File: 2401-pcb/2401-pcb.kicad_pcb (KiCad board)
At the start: 2 copper layers, 33 parts, among them J1 Conn_01x04_Female, Q1 SFH3710, Q2 SFH3710, SW1 SW_SPDT, U1 TLV70228_SOT23-5, U2 VL6180X, U3 LIS3DH, U4 LMV321, U5 LMV321, U6 INA126, U7 DPS422, U8 AT25SF641-SUB-T, U9 STM32G070KBT6

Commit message: Improve schematics
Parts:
- removed the C6 at (135.9, 108.6)
- added C13: 4.7uF, Capacitor_SMD:C_0805_2012Metric, F.Cu at (175.0, 106.0)
- added C14: 100nF, Capacitor_SMD:C_0603_1608Metric, F.Cu at (170.0, 80.0)
- added C3: 100nF, Capacitor_SMD:C_0603_1608Metric, F.Cu at (165.0, 123.0)
- added C5: CP1_Small, Capacitor_SMD:CP_Elec_4x5.4, F.Cu at (159.1, 124.7)
- added D3: Red, LED_SMD:LED_0805_2012Metric, F.Cu at (165.8, 80.2)
- added D4: Green, LED_SMD:LED_0805_2012Metric, F.Cu at (170.5, 77.2)
- added J2: Conn_ARM_JTAG_SWD_10, Jitter_Footprints:connector_jtag_10pin_shrouded, F.Cu at (89.0, 107.0)
- added J3: Conn_01x04_Male, Connector_PinHeader_2.54mm:PinHeader_1x04_P2.54mm_Vertical, F.Cu at (178.0, 124.0)
- added R10: 4k7, Resistor_SMD:R_0805_2012Metric_Pad1.15x1.40mm_HandSolder, F.Cu at (161.2, 80.1)
- added R11: 150, Resistor_SMD:R_0805_2012Metric_Pad1.15x1.40mm_HandSolder, F.Cu at (165.9, 77.2)
- added R12: 150, Resistor_SMD:R_0805_2012Metric_Pad1.15x1.40mm_HandSolder, F.Cu at (170.7, 74.2)
- added R3: 47k, Resistor_SMD:R_0805_2012Metric_Pad1.15x1.40mm_HandSolder, F.Cu at (169.0, 113.0)
- added R4: 47k, Resistor_SMD:R_0805_2012Metric_Pad1.15x1.40mm_HandSolder, F.Cu at (173.8, 113.0)
- added R7: 4k7, Resistor_SMD:R_0805_2012Metric_Pad1.15x1.40mm_HandSolder, F.Cu at (161.2, 74.2)
- added R8: 4k7, Resistor_SMD:R_0805_2012Metric_Pad1.15x1.40mm_HandSolder, F.Cu at (161.2, 77.2)
- added R9: 4k7, Resistor_SMD:R_0805_2012Metric_Pad1.15x1.40mm_HandSolder, F.Cu at (165.9, 74.2)
- C2: value 100nF -> 4.7uF; footprint Capacitor_SMD:C_0603_1608Metric -> Capacitor_SMD:C_0805_2012Metric
- moved U8 5.00 mm to (164.0, 97.0)
- renumbered C8 to C10, C3 to C11, C4 to C12, C12 to C15, C5 to C4, C11 to C6, C9 to C8, C10 to C9, R3 to R5, R4 to R6, U3 to U1, U6 to U3, U7 to U5, U5 to U6, U1 to U7, U9 to U8, U8 to U9
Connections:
- net Net-(BT1-Pad1) renamed Vbatt
- U1 pad 11: (no net) -> /accel_int1
- U1 pad 4: (no net) -> /SCL
- U1 pad 6: (no net) -> /SDA
- U1 pad 8: (no net) -> +2V8
- U1 pad 9: (no net) -> /accel_int2
- U2 pad 1: (no net) -> /distance_int
- U2 pad 4: (no net) -> Net-(R3-Pad2)
- U2 pad 5: (no net) -> /SCL
- U2 pad 6: (no net) -> /SDA
- U3 pad 6: (no net) -> /load_cell
- U4 pad 2: +2V8 -> GND
- U4 pad 5: GND -> +2V8
- U5 pad 2: (no net) -> +2V8
- U5 pad 3: (no net) -> /SDA
- U5 pad 4: (no net) -> /SCL
- U5 pad 5: (no net) -> GND
- U6 pad 2: +2V8 -> GND
- U6 pad 5: GND -> +2V8
- U8 pad 1: (no net) -> /LED_RED
- U8 pad 10: (no net) -> /photo_diode_2
- U8 pad 11: (no net) -> /load_cell
- U8 pad 12: (no net) -> /FLASH_SCLK
- U8 pad 13: (no net) -> /FLASH_MISO
- U8 pad 14: (no net) -> /FLASH_MOSI
- U8 pad 15: (no net) -> /Vbatt_sense
- U8 pad 16: (no net) -> /distance_int
- U8 pad 17: (no net) -> /accel_int1
- U8 pad 18: (no net) -> /~FLASH_CS
- U8 pad 19: (no net) -> /Tx
- U8 pad 21: (no net) -> /Rx
- U8 pad 24: (no net) -> /SWDIO
- U8 pad 25: (no net) -> /SWCLK
- U8 pad 27: (no net) -> /accel_int2
- U8 pad 30: (no net) -> /SCL
- U8 pad 31: (no net) -> /SDA
- U8 pad 32: (no net) -> /LED_GREEN
- U8 pad 4: (no net) -> +2V8
- U8 pad 5: (no net) -> GND
- U8 pad 6: (no net) -> /~RST
- U8 pad 7: (no net) -> /photo_transistor_1
- U8 pad 8: (no net) -> /photo_transistor_2
- U8 pad 9: (no net) -> /photo_diode_1
- U9 pad 1: (no net) -> /~FLASH_CS
- U9 pad 2: (no net) -> /FLASH_MISO
- U9 pad 3: (no net) -> +2V8
- U9 pad 5: (no net) -> /FLASH_MOSI
- U9 pad 6: (no net) -> /FLASH_SCLK
- U9 pad 7: (no net) -> +2V8

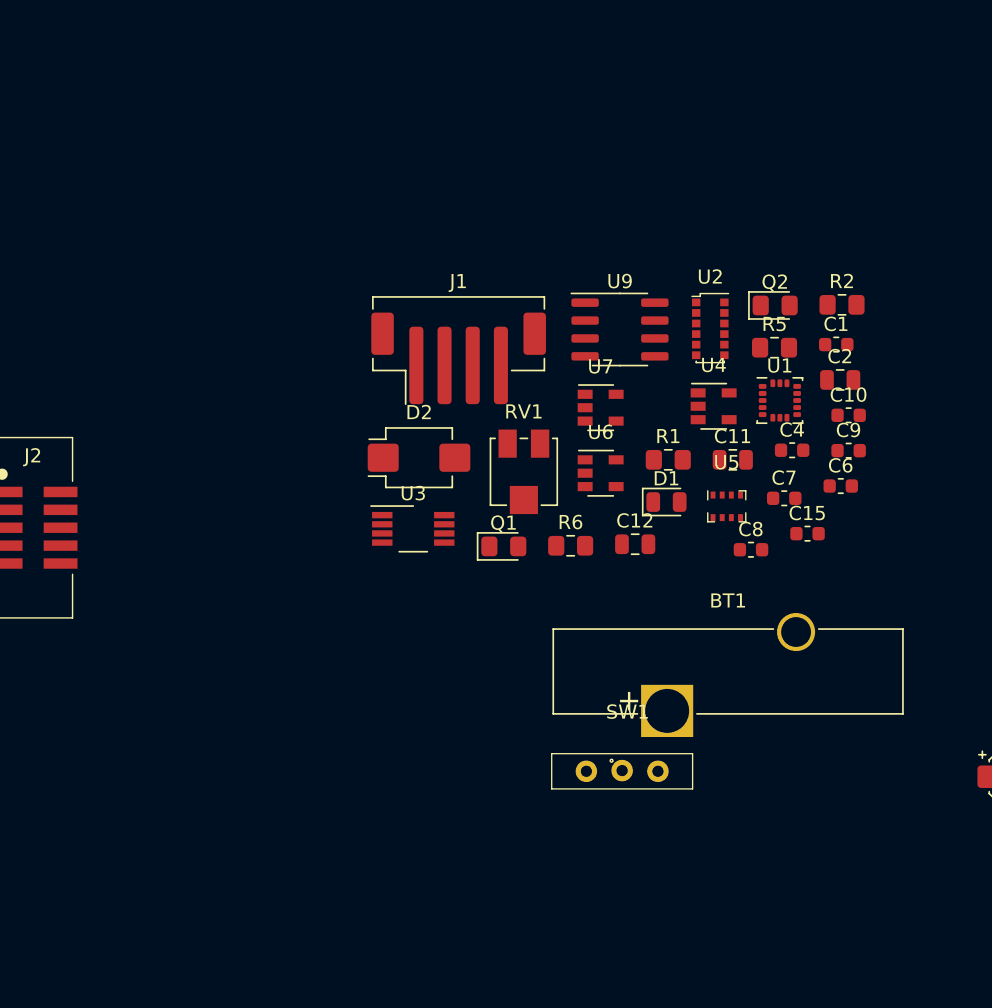
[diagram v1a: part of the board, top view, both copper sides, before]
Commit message: PCB: assign/fix footprints + 3D
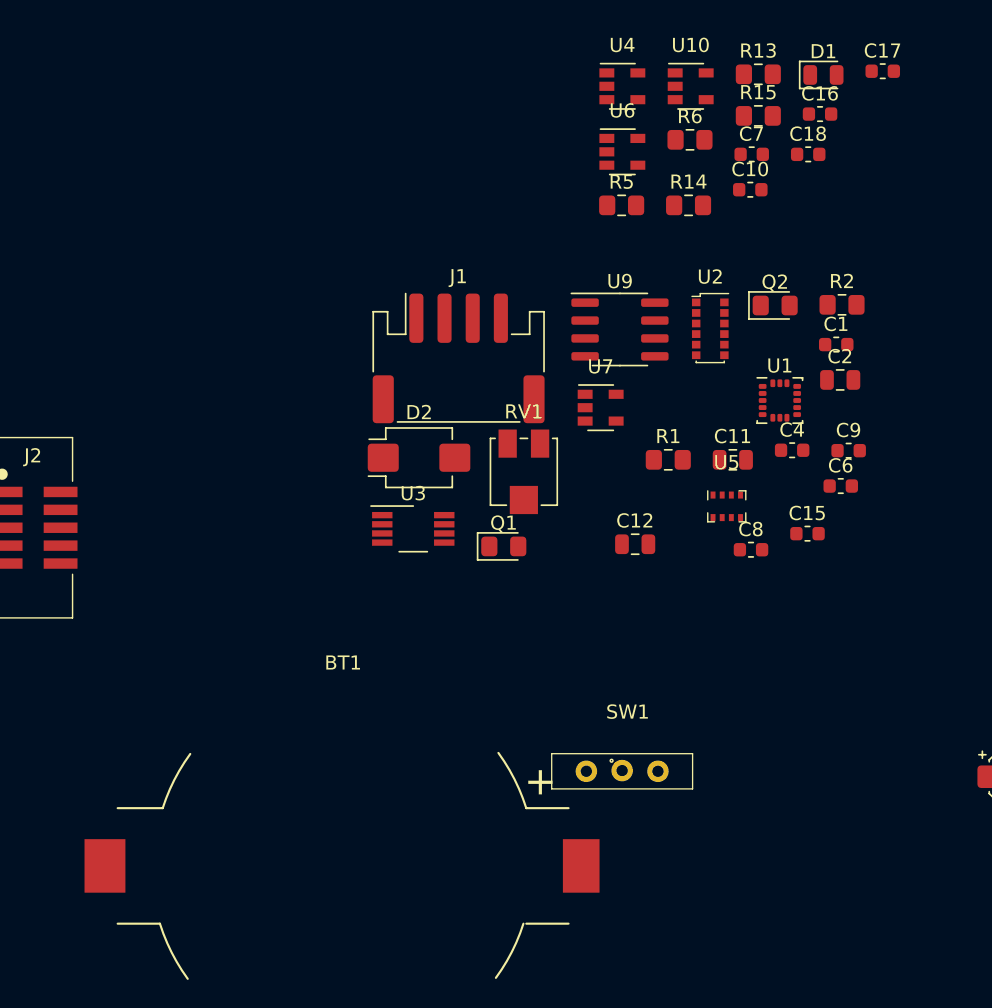
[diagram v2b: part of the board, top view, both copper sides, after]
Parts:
- added C16: 100nF, Capacitor_SMD:C_0603_1608Metric, F.Cu at (144.8, 77.6)
- added C17: 15pF, Capacitor_SMD:C_0603_1608Metric, F.Cu at (149.3, 74.6)
- added C18: 100nF, Capacitor_SMD:C_0603_1608Metric, F.Cu at (144.0, 80.5)
- added R13: 0, Resistor_SMD:R_0805_2012Metric_Pad1.15x1.40mm_HandSolder, F.Cu at (140.5, 74.8)
- added R14: 10M, Resistor_SMD:R_0805_2012Metric_Pad1.15x1.40mm_HandSolder, F.Cu at (135.5, 84.1)
- added R15: 0, Resistor_SMD:R_0805_2012Metric_Pad1.15x1.40mm_HandSolder, F.Cu at (140.5, 77.8)
- added U10: MCP6001U, Package_TO_SOT_SMD:SOT-23-5, F.Cu at (135.7, 75.7)
- BT1: value Battery_Cell -> SMTU 2450N-1-LF; footprint Battery:Battery_Panasonic_CR2450-VAN_Vertical_CircularHoles -> Jitter_Footprints:BatteryHolder_SMTU-2450N-1-LF_1x2450
- C10: value 100nF -> 15pF
- C5: value CP1_Small -> 10uF
- J1: value Conn_01x04_Female -> Load Cell; footprint Connector_JST:JST_PH_B4B-PH-SM4-TB_1x04-1MP_P2.00mm_Vertical -> Jitter_Footprints:JST_PH_S4B-PH-SM4-TB_1x04-1MP_P2.00mm_Horizontal
- R1, R2, R6: value R -> 10M
- R10, R9: value 4k7 -> 47k
- R5: value R -> DNI
- U4, U6: value LMV321 -> MCP6001U
- moved D1 32.3 mm to (145.1, 74.9)
- moved R6 30.0 mm to (135.6, 79.5)
- moved BT1 25.5 mm to (111.0, 131.0)
- moved C7 24.5 mm to (140.0, 80.5)
- moved U4 23.6 mm to (130.8, 75.7)
- moved U6 22.9 mm to (130.8, 80.3)
- moved C10 17.5 mm to (139.9, 83.0)
- moved R5 14.8 mm to (130.8, 84.1)
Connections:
- C10 pad 1: +2V8 -> /photo_diode_1
- C10 pad 2: GND -> Net-(C10-Pad2)
- D1 pad 1: Net-(D1-Pad1) -> Net-(C10-Pad2)
- D1 pad 2: GND -> Net-(D1-Pad2)
- D2 pad 1: Net-(D2-Pad1) -> Net-(C17-Pad2)
- D2 pad 2: GND -> Net-(D2-Pad2)
- J1 pad MP: (no net) -> GND
- Q2 pad 1: /photo_transistor_2 -> Net-(Q2-Pad1)
- R2 pad 2: /photo_transistor_2 -> Net-(Q2-Pad1)
- R5 pad 1: /photo_diode_1 -> /photo_transistor_2
- R5 pad 2: Net-(D1-Pad1) -> Net-(Q2-Pad1)
- R6 pad 1: /photo_diode_2 -> /photo_diode_1
- R6 pad 2: Net-(D2-Pad1) -> Net-(C10-Pad2)
- U4 pad 1: GND -> Net-(Q2-Pad1)
- U4 pad 3: Net-(D1-Pad1) -> /photo_transistor_2
- U4 pad 4: /photo_diode_1 -> /photo_transistor_2
- U6 pad 1: GND -> Net-(D1-Pad2)
- U6 pad 3: Net-(D2-Pad1) -> Net-(C10-Pad2)
- U6 pad 4: /photo_diode_2 -> /photo_diode_1

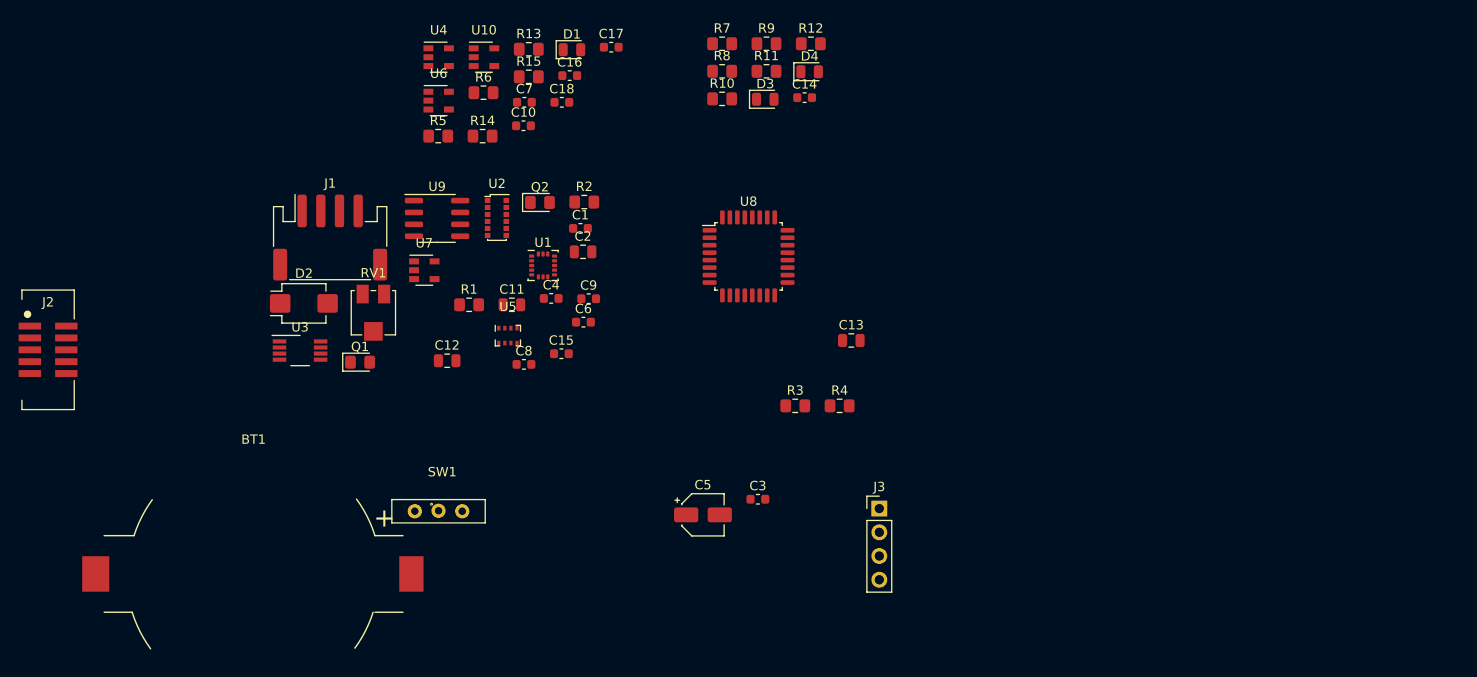
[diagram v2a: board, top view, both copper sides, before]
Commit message: PCB: routing is more or less done
The KiCAD DRC passes, but it is not checked againts the Jitter
Checklist..
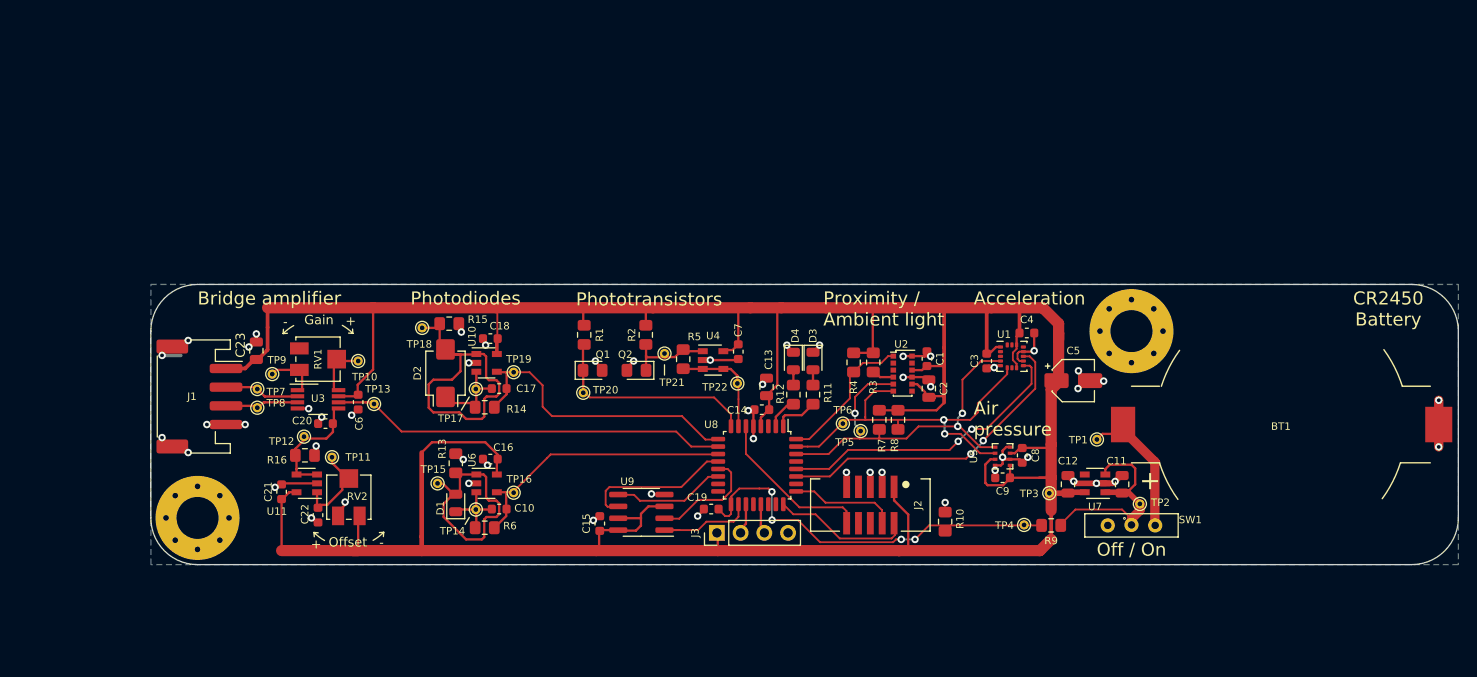
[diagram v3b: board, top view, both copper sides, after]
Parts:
- added C19: 100nF, Capacitor_SMD:C_0603_1608Metric, F.Cu at (160.0, 124.0)
- added C20: 100nF, Capacitor_SMD:C_0603_1608Metric, F.Cu at (118.7, 114.9)
- added C21: 100nF, Capacitor_SMD:C_0603_1608Metric, F.Cu at (114.0, 122.2)
- added C22: 100nF, Capacitor_SMD:C_0603_1608Metric, F.Cu at (117.9, 124.7)
- added C23: 4.7uF, Capacitor_SMD:C_0805_2012Metric, F.Cu at (111.3, 107.1)
- added H1: MountingHole_Pad, MountingHole:MountingHole_4.5mm_Pad_Via, F.Cu at (105.0, 125.0)
- added H2: MountingHole_Pad, MountingHole:MountingHole_4.5mm_Pad_Via, F.Cu at (205.0, 105.0)
- added R16: DNI, Resistor_SMD:R_0805_2012Metric_Pad1.15x1.40mm_HandSolder, F.Cu at (116.5, 118.3)
- added RV2: 100KΩ, Potentiometer_SMD:Potentiometer_Bourns_3314J_Vertical, F.Cu at (121.2, 122.8)
- added TP1: DNI, TestPoint:TestPoint_THTPad_D1.0mm_Drill0.5mm, F.Cu at (201.3, 116.6)
- added TP10: DNI, TestPoint:TestPoint_THTPad_D1.0mm_Drill0.5mm, F.Cu at (122.2, 108.2)
- added TP11: DNI, TestPoint:TestPoint_THTPad_D1.0mm_Drill0.5mm, F.Cu at (119.4, 118.5)
- added TP12: DNI, TestPoint:TestPoint_THTPad_D1.0mm_Drill0.5mm, F.Cu at (116.4, 116.3)
- added TP13: DNI, TestPoint:TestPoint_THTPad_D1.0mm_Drill0.5mm, F.Cu at (123.9, 112.8)
- added TP14: DNI, TestPoint:TestPoint_THTPad_D1.0mm_Drill0.5mm, F.Cu at (134.8, 124.1)
- added TP15: DNI, TestPoint:TestPoint_THTPad_D1.0mm_Drill0.5mm, F.Cu at (130.7, 121.3)
- added TP16: DNI, TestPoint:TestPoint_THTPad_D1.0mm_Drill0.5mm, F.Cu at (138.8, 122.3)
- added TP17: DNI, TestPoint:TestPoint_THTPad_D1.0mm_Drill0.5mm, F.Cu at (134.8, 111.2)
- added TP18: DNI, TestPoint:TestPoint_THTPad_D1.0mm_Drill0.5mm, F.Cu at (129.1, 104.7)
- added TP19: DNI, TestPoint:TestPoint_THTPad_D1.0mm_Drill0.5mm, F.Cu at (138.8, 109.4)
- added TP2: DNI, TestPoint:TestPoint_THTPad_D1.0mm_Drill0.5mm, F.Cu at (205.9, 123.5)
- added TP20: DNI, TestPoint:TestPoint_THTPad_D1.0mm_Drill0.5mm, F.Cu at (146.3, 111.6)
- added TP21: DNI, TestPoint:TestPoint_THTPad_D1.0mm_Drill0.5mm, F.Cu at (155.0, 107.4)
- added TP22: DNI, TestPoint:TestPoint_THTPad_D1.0mm_Drill0.5mm, F.Cu at (162.8, 110.6)
- added TP3: DNI, TestPoint:TestPoint_THTPad_D1.0mm_Drill0.5mm, F.Cu at (196.2, 122.3)
- added TP4: DNI, TestPoint:TestPoint_THTPad_D1.0mm_Drill0.5mm, F.Cu at (193.5, 125.8)
- added TP5: DNI, TestPoint:TestPoint_THTPad_D1.0mm_Drill0.5mm, F.Cu at (176.0, 115.7)
- added TP6: DNI, TestPoint:TestPoint_THTPad_D1.0mm_Drill0.5mm, F.Cu at (174.1, 114.9)
- added TP7: DNI, TestPoint:TestPoint_THTPad_D1.0mm_Drill0.5mm, F.Cu at (111.4, 111.2)
- added TP8: DNI, TestPoint:TestPoint_THTPad_D1.0mm_Drill0.5mm, F.Cu at (111.4, 113.2)
- added TP9: DNI, TestPoint:TestPoint_THTPad_D1.0mm_Drill0.5mm, F.Cu at (113.0, 109.6)
- added U11: MCP6001U, Package_TO_SOT_SMD:SOT-23-5, F.Cu at (116.7, 121.3)
- moved BT1 111.2 mm to (221.0, 115.0), turned to 180 degrees
- moved J2 89.6 mm to (177.0, 123.6), turned to 270 degrees
- moved U7 75.4 mm to (201.1, 121.3), turned to 180 degrees
- moved SW1 74.2 mm to (205.0, 125.8)
- moved C11 68.1 mm to (204.0, 121.4), turned to 90 degrees
- moved C12 67.8 mm to (198.2, 121.4), turned to 90 degrees
- moved R9 59.9 mm to (196.4, 125.8), turned to 180 degrees
- moved U5 54.5 mm to (191.2, 118.4), turned to 90 degrees
- moved C8 54.2 mm to (193.3, 118.3), turned to 270 degrees
- moved R10 51.2 mm to (185.1, 125.4), turned to 90 degrees
- moved U1 51.1 mm to (192.2, 107.7)
- moved C4 51.1 mm to (193.8, 105.2)
- moved D1 50.1 mm to (132.7, 123.4), turned to 90 degrees
- moved C9 48.3 mm to (191.2, 120.7), turned to 180 degrees
- moved R6 46.6 mm to (135.8, 126.0), turned to 180 degrees
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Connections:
- net Net-(C10-Pad2) renamed /D1_V-
- net Net-(C17-Pad2) renamed /D2_V-
- net Net-(D1-Pad2) renamed /D1_V+
- net Net-(D2-Pad2) renamed /D2_V+
- BT1 pad 1: Vbatt -> Net-(BT1-Pad1)
- C11 pad 1: Net-(C11-Pad1) -> Vbatt
- J1 pad 2: /load_cell_out+ -> /load_cell_out-
- J1 pad 3: /load_cell_out- -> /load_cell_out+
- RV1 pad 1: Net-(RV1-Pad1) -> (no net)
- RV1 pad 3: (no net) -> Net-(RV1-Pad3)
- SW1 pad 1: Net-(C11-Pad1) -> Vbatt
- SW1 pad 2: Vbatt -> Net-(BT1-Pad1)
- U3 pad 1: Net-(RV1-Pad1) -> Net-(RV1-Pad3)
- U3 pad 5: GND -> /load_cell_ref
- U7 pad 1: Net-(C11-Pad1) -> Vbatt
- U7 pad 3: Net-(C11-Pad1) -> Vbatt
- U8 pad 10: /photo_diode_2 -> /load_cell
- U8 pad 11: /load_cell -> /photo_diode_1
- U8 pad 15: /Vbatt_sense -> (no net)
- U8 pad 16: /distance_int -> (no net)
- U8 pad 17: /accel_int1 -> /Vbatt_sense
- U8 pad 2: (no net) -> /LED_GREEN
- U8 pad 27: /accel_int2 -> /accel_int1
- U8 pad 28: (no net) -> /accel_int2
- U8 pad 32: /LED_GREEN -> /distance_int
- U8 pad 7: /photo_transistor_1 -> /photo_transistor_2
- U8 pad 8: /photo_transistor_2 -> /photo_transistor_1
- U8 pad 9: /photo_diode_1 -> /photo_diode_2
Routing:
- net +2V8: track 0.00 -> 367.6 mm
- net GND: track 0.00 -> 95.1 mm, vias 0 -> 53
- net /SCL: track 0.00 -> 43.6 mm, vias 0 -> 3
- net /Vbatt_sense: track 0.00 -> 42.8 mm, vias 0 -> 4
- net /load_cell: track 0.00 -> 42.6 mm
- net /SDA: track 0.00 -> 41.3 mm, vias 0 -> 2
- net /accel_int1: track 0.00 -> 33.9 mm, vias 0 -> 2
- net /D2_V+: track 0.00 -> 33.8 mm
- net /photo_diode_2: track 0.00 -> 32.4 mm
- net /accel_int2: track 0.00 -> 31.7 mm, vias 0 -> 2
- net /photo_diode_1: track 0.00 -> 29.6 mm
- net /D1_V+: track 0.00 -> 24.8 mm
- net /photo_transistor_1: track 0.00 -> 23.1 mm
- net Vbatt: track 0.00 -> 22.8 mm
- net /~RST: track 0.00 -> 17.6 mm
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- added copper zone on B.Cu, net GND
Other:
- board outline added: 140 x 30 mm
- net class Default: clearance 0.2 -> 0.15
- rule pad_to_mask_clearance: 0.051 -> 0.04
- rule solder_mask_min_width: 0.25 -> 0.07
- rule trace_clearance: 0.2 -> 0.15
- board text added: "+"
- board text added: "-"
- board text added: "Acceleration"
- board text added: "Air pressure"
- board text added: "Bridge amplifier"
- board text added: "CR2450 Battery"
- board text added: "Gain"
- board text added: "Off / On"
- board text added: "Offset"
- board text added: "Photodiodes"
- board text added: "Phototransistors"
- board text added: "Proximity / Ambient light"

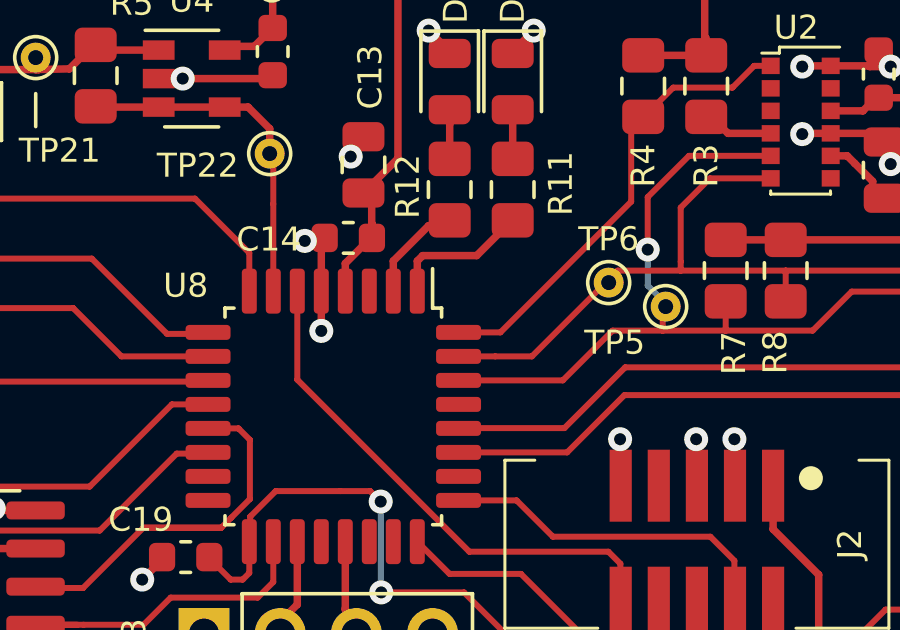
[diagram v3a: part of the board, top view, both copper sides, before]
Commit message: Schematics: remap LED pins: PC13-15 are low-current only
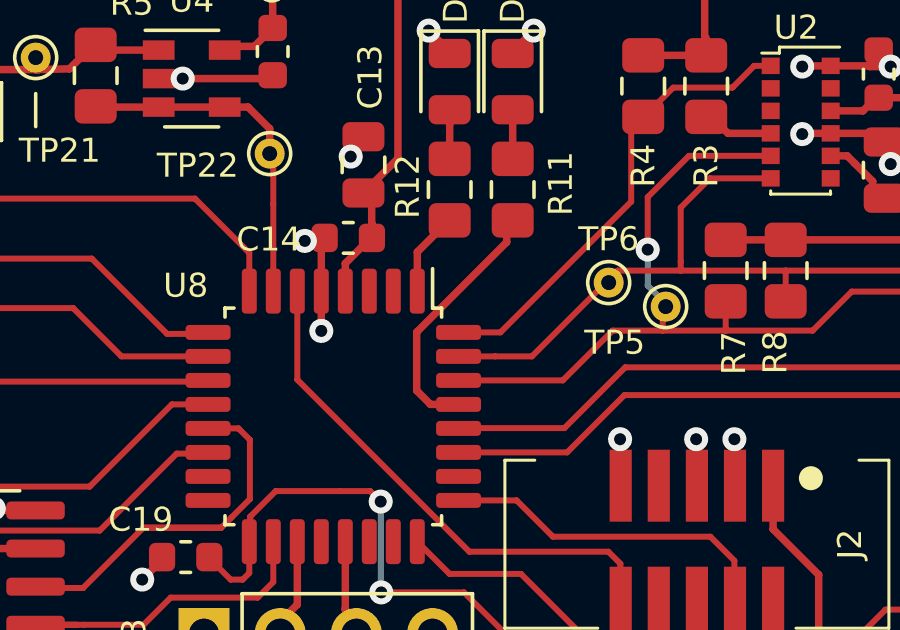
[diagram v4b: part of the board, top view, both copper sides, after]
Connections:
- U8 pad 1: /LED_RED -> /LED_GREEN
- U8 pad 2: /LED_GREEN -> (no net)
- U8 pad 29: (no net) -> /LED_RED
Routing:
- net /LED_RED: track 4.47 -> 8.43 mm
- net /LED_GREEN: track 3.37 -> 2.66 mm
